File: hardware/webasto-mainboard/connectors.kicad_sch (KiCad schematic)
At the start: 7 parts, among them J3 2-pole connector

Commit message: Update title block on mainboard, print PDFs
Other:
- company: (none) -> Gavin Hurlbut
- title: Webasto Thermo Top C Replacement Controller -> Webasto Replacement Mainboard (Thermo Top C)
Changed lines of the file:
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@@
   (paper "A4")
   (title_block
-    (title "Webasto Thermo Top C Replacement Controller")
-    (date "2023-01-19")
+    (title "Webasto Replacement Mainboard (Thermo Top C)")
+    (date "2023-01-31")
     (rev "v1.0")
+    (company "Gavin Hurlbut")
   )
   (junction (at 141.732 120.015) (diameter 0) (color 0 0 0 0)

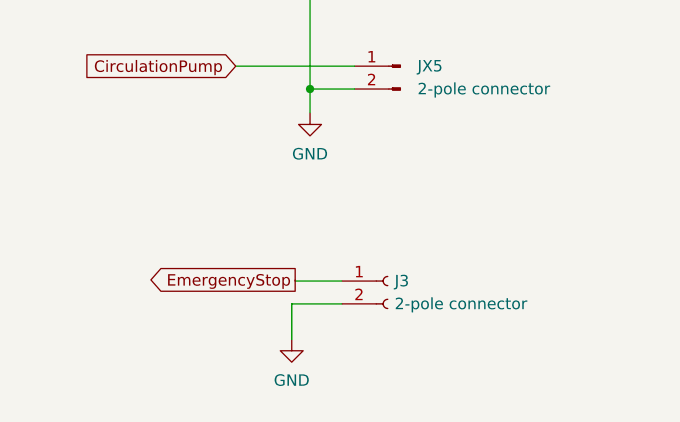
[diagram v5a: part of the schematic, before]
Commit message: Moved emerg. shutdown offboard
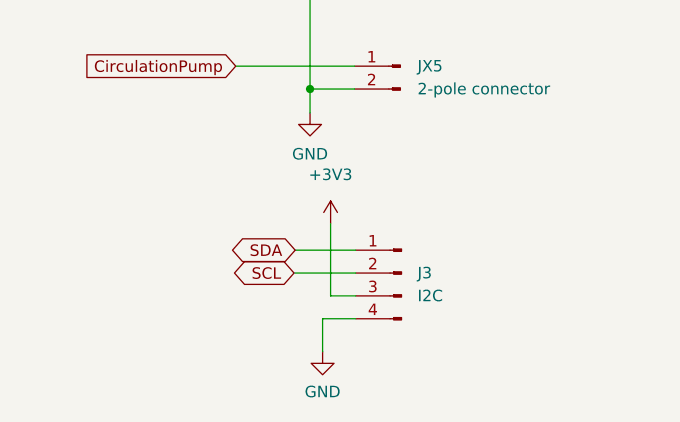
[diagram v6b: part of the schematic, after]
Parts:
- removed J3: 2-pole connector, Connector_PinHeader_2.54mm:PinHeader_1x02_P2.54mm_Horizontal, symbol Connector:Conn_01x02_Female
- added J3: I2C, Connector_PinHeader_2.54mm:PinHeader_1x04_P2.54mm_Vertical, symbol Connector:Conn_01x04_Male
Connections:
- net GND: now also J3.4 (Pin_4)
- net SCL: now also J3.2 (Pin_2)
- net SDA: now also J3.1 (Pin_1)
- new net +3V3: J3.3 (Pin_3)
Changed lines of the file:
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@@
   (title_block
     (title "Webasto Replacement Mainboard (Thermo Top C)")
-    (date "2023-01-31")
-    (rev "v1.0")
+    (date "2023-02-10")
+    (rev "2.0")
     (company "Gavin Hurlbut")
   )
@@
     (stroke (width 0) (type default) (color 0 0 0 0))
   )
+  (wire (pts (xy 146.812 143.002) (xy 144.018 143.002))
+    (stroke (width 0) (type default) (color 0 0 0 0))
+  )
   (wire (pts (xy 131.699 89.662) (xy 145.288 89.662))
     (stroke (width 0) (type default) (color 0 0 0 0))
   )
-  (wire (pts (xy 139.7 143.891) (xy 145.288 143.891))
-    (stroke (width 0) (type default) (color 0 0 0 0))
-  )
   (wire (pts (xy 133.223 105.664) (xy 146.558 105.664))
     (stroke (width 0) (type default) (color 0 0 0 0))
   )
-  (wire (pts (xy 139.7 143.891) (xy 139.7 147.828))
+  (wire (pts (xy 146.812 145.542) (xy 143.129 145.542))
     (stroke (width 0) (type default) (color 0 0 0 0))
   )
@@
     (stroke (width 0) (type default) (color 0 0 0 0))
   )
-  (wire (pts (xy 145.288 141.351) (xy 140.081 141.351))
+  (wire (pts (xy 139.954 140.462) (xy 146.812 140.462))
     (stroke (width 0) (type default) (color 0 0 0 0))
   )
@@
     (stroke (width 0) (type default) (color 0 0 0 0))
   )
+  (wire (pts (xy 144.018 143.002) (xy 144.018 135.001))
+    (stroke (width 0) (type default) (color 0 0 0 0))
+  )
   (wire (pts (xy 141.732 108.204) (xy 146.558 108.204))
     (stroke (width 0) (type default) (color 0 0 0 0))
@@
     (stroke (width 0) (type default) (color 0 0 0 0))
   )
-  (wire (pts (xy 140.081 141.351) (xy 140.081 141.224))
-    (stroke (width 0) (type default) (color 0 0 0 0))
-  )
   (wire (pts (xy 131.699 92.202) (xy 145.288 92.202))
     (stroke (width 0) (type default) (color 0 0 0 0))
@@
     (stroke (width 0) (type default) (color 0 0 0 0))
   )
+  (wire (pts (xy 143.129 145.542) (xy 143.129 149.225))
+    (stroke (width 0) (type default) (color 0 0 0 0))
+  )
   (wire (pts (xy 126.238 73.025) (xy 112.268 73.025))
     (stroke (width 0) (type default) (color 0 0 0 0))
@@
     (stroke (width 0) (type default) (color 0 0 0 0))
   )
+  (wire (pts (xy 140.081 137.922) (xy 146.812 137.922))
+    (stroke (width 0) (type default) (color 0 0 0 0))
+  )
+  (global_label "SCL" (shape bidirectional) (at 139.954 140.462 180) (fields_autoplaced)
+    (effects (font (size 1.27 1.27)) (justify right))
+    (property "Intersheet References" "${INTERSHEET_REFS}" (id 0) (at 134.0333 140.3826 0)
+      (effects (font (size 1.27 1.27)) (justify right) hide)
+    )
+  )
   (global_label "CirculationPump" (shape input) (at 133.477 117.475 180) (fields_autoplaced)
     (effects (font (size 1.27 1.27)) (justify right))
@@
     (effects (font (size 1.27 1.27)) (justify right))
     (property "Intersheet References" "${INTERSHEET_REFS}" (id 0) (at 119.7004 60.6266 0)
+      (effects (font (size 1.27 1.27)) (justify right) hide)
+    )
+  )
+  (global_label "SDA" (shape bidirectional) (at 140.081 137.922 180) (fields_autoplaced)
+    (effects (font (size 1.27 1.27)) (justify right))
+    (property "Intersheet References" "${INTERSHEET_REFS}" (id 0) (at 134.0998 137.8426 0)
       (effects (font (size 1.27 1.27)) (justify right) hide)
     )
@@
     (property "Intersheet References" "${INTERSHEET_REFS}" (id 0) (at 171.178 63.1666 0)
       (effects (font (size 1.27 1.27)) (justify left) hide)
-    )
-  )
-  (global_label "EmergencyStop" (shape output) (at 140.081 141.224 180) (fields_autoplaced)
-    (effects (font (size 1.27 1.27)) (justify right))
-    (property "Intersheet References" "${INTERSHEET_REFS}" (id 0) (at 123.2746 141.1446 0)
-      (effects (font (size 1.27 1.27)) (justify right) hide)
     )
   )
@@
     (pin "6")
   )
+  (symbol (lib_id "power:GND") (at 143.129 149.225 0) (unit 1)
+    (in_bom yes) (on_board yes) (fields_autoplaced)
+    (property "Reference" "#PWR024" (id 0) (at 143.129 155.575 0)
+      (effects (font (size 1.27 1.27)) hide)
+    )
+    (property "Value" "GND" (id 1) (at 143.129 153.67 0))
+    (property "Footprint" "" (id 2) (at 143.129 149.225 0)
+      (effects (font (size 1.27 1.27)) hide)
+    )
+    (property "Datasheet" "" (id 3) (at 143.129 149.225 0)
+      (effects (font (size 1.27 1.27)) hide)
+    )
+    (pin "1")
+  )
   (symbol (lib_id "Device:Polyfuse") (at 130.048 73.025 90) (unit 1)
     (in_bom yes) (on_board yes) (fields_autoplaced)
@@
   (symbol (lib_id "power:GND") (at 141.732 122.682 0) (unit 1)
     (in_bom yes) (on_board yes) (fields_autoplaced)
-    (property "Reference" "#PWR024" (id 0) (at 141.732 129.032 0)
+    (property "Reference" "#PWR023" (id 0) (at 141.732 129.032 0)
       (effects (font (size 1.27 1.27)) hide)
     )
@@
     (pin "1")
   )
+  (symbol (lib_id "Connector:Conn_01x04_Male") (at 151.892 140.462 0) (mirror y) (unit 1)
+    (in_bom yes) (on_board yes) (fields_autoplaced)
+    (property "Reference" "J3" (id 0) (at 153.67 140.4619 0)
+      (effects (font (size 1.27 1.27)) (justify right))
+    )
+    (property "Value" "I2C" (id 1) (at 153.67 143.0019 0)
+      (effects (font (size 1.27 1.27)) (justify right))
+    )
+    (property "Footprint" "Connector_PinHeader_2.54mm:PinHeader_1x04_P2.54mm_Vertical" (id 2) (at 151.892 140.462 0)
+      (effects (font (size 1.27 1.27)) hide)
+    )
+    (property "Datasheet" "~" (id 3) (at 151.892 140.462 0)
+      (effects (font (size 1.27 1.27)) hide)
+    )
+    (pin "1")
+    (pin "2")
+    (pin "3")
+    (pin "4")
+  )
+  (symbol (lib_id "power:+3V3") (at 144.018 135.001 0) (unit 1)
+    (in_bom yes) (on_board yes) (fields_autoplaced)
+    (property "Reference" "#PWR025" (id 0) (at 144.018 138.811 0)
+      (effects (font (size 1.27 1.27)) hide)
+    )
+    (property "Value" "+3V3" (id 1) (at 144.018 129.54 0))
+    (property "Footprint" "" (id 2) (at 144.018 135.001 0)
+      (effects (font (size 1.27 1.27)) hide)
+    )
+    (property "Datasheet" "" (id 3) (at 144.018 135.001 0)
+      (effects (font (size 1.27 1.27)) hide)
+    )
+    (pin "1")
+  )
   (symbol (lib_id "power:GND") (at 139.319 77.978 0) (unit 1)
     (in_bom yes) (on_board yes) (fields_autoplaced)
@@
       (effects (font (size 1.27 1.27)) hide)
     )
-    (pin "1")
-  )
-  (symbol (lib_id "Connector:Conn_01x02_Female") (at 150.368 141.351 0) (unit 1)
-    (in_bom yes) (on_board yes) (fields_autoplaced)
-    (property "Reference" "J3" (id 0) (at 151.13 141.3509 0)
-      (effects (font (size 1.27 1.27)) (justify left))
-    )
-    (property "Value" "2-pole connector" (id 1) (at 151.13 143.8909 0)
-      (effects (font (size 1.27 1.27)) (justify left))
-    )
-    (property "Footprint" "Connector_PinHeader_2.54mm:PinHeader_1x02_P2.54mm_Horizontal" (id 2) (at 150.368 141.351 0)
-      (effects (font (size 1.27 1.27)) hide)
-    )
-    (property "Datasheet" "~" (id 3) (at 150.368 141.351 0)
-      (effects (font (size 1.27 1.27)) hide)
-    )
-    (pin "1")
-    (pin "2")
-  )
-  (symbol (lib_id "power:GND") (at 139.7 147.828 0) (unit 1)
-    (in_bom yes) (on_board yes) (fields_autoplaced)
-    (property "Reference" "#PWR023" (id 0) (at 139.7 154.178 0)
-      (effects (font (size 1.27 1.27)) hide)
-    )
-    (property "Value" "GND" (id 1) (at 139.7 152.4 0))
-    (property "Footprint" "" (id 2) (at 139.7 147.828 0)
-      (effects (font (size 1.27 1.27)) hide)
-    )
-    (property "Datasheet" "" (id 3) (at 139.7 147.828 0)
-      (effects (font (size 1.27 1.27)) hide)
-    )

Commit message: Got rid of TINY diode (0402!?!?), remove USE_USB, put in PicoW
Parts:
- renumbered J3 to J2
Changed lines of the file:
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@@
   (title_block
     (title "Webasto Replacement Mainboard (Thermo Top C)")
-    (date "2023-02-10")
+    (date "2023-02-14")
     (rev "2.0")
     (company "Gavin Hurlbut")
@@
   (symbol (lib_id "power:GND") (at 143.129 149.225 0) (unit 1)
     (in_bom yes) (on_board yes) (fields_autoplaced)
-    (property "Reference" "#PWR024" (id 0) (at 143.129 155.575 0)
+    (property "Reference" "#PWR022" (id 0) (at 143.129 155.575 0)
       (effects (font (size 1.27 1.27)) hide)
     )
@@
   (symbol (lib_id "power:+12V") (at 112.268 67.31 0) (unit 1)
     (in_bom yes) (on_board yes) (fields_autoplaced)
-    (property "Reference" "#PWR021" (id 0) (at 112.268 71.12 0)
+    (property "Reference" "#PWR019" (id 0) (at 112.268 71.12 0)
       (effects (font (size 1.27 1.27)) hide)
     )
@@
   (symbol (lib_id "power:GND") (at 141.732 122.682 0) (unit 1)
     (in_bom yes) (on_board yes) (fields_autoplaced)
-    (property "Reference" "#PWR023" (id 0) (at 141.732 129.032 0)
+    (property "Reference" "#PWR021" (id 0) (at 141.732 129.032 0)
       (effects (font (size 1.27 1.27)) hide)
     )
@@
   (symbol (lib_id "Connector:Conn_01x04_Male") (at 151.892 140.462 0) (mirror y) (unit 1)
     (in_bom yes) (on_board yes) (fields_autoplaced)
-    (property "Reference" "J3" (id 0) (at 153.67 140.4619 0)
+    (property "Reference" "J2" (id 0) (at 153.67 140.4619 0)
       (effects (font (size 1.27 1.27)) (justify right))
     )
@@
   (symbol (lib_id "power:+3V3") (at 144.018 135.001 0) (unit 1)
     (in_bom yes) (on_board yes) (fields_autoplaced)
-    (property "Reference" "#PWR025" (id 0) (at 144.018 138.811 0)
+    (property "Reference" "#PWR023" (id 0) (at 144.018 138.811 0)
       (effects (font (size 1.27 1.27)) hide)
     )
@@
   (symbol (lib_id "power:GND") (at 139.319 77.978 0) (unit 1)
     (in_bom yes) (on_board yes) (fields_autoplaced)
-    (property "Reference" "#PWR022" (id 0) (at 139.319 84.328 0)
-      (effects (font (size 1.27 1.27)) hide)
-    )
+    (property "Reference" "#PWR020" (id 0) (at 139.319 84.328 0)
+      (effects (font (size 1.27 1.27)) hide)
+    )
